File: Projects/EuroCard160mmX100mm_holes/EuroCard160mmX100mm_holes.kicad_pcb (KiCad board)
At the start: 2 copper layers, 159.9 x 99.9 mm, 4 parts

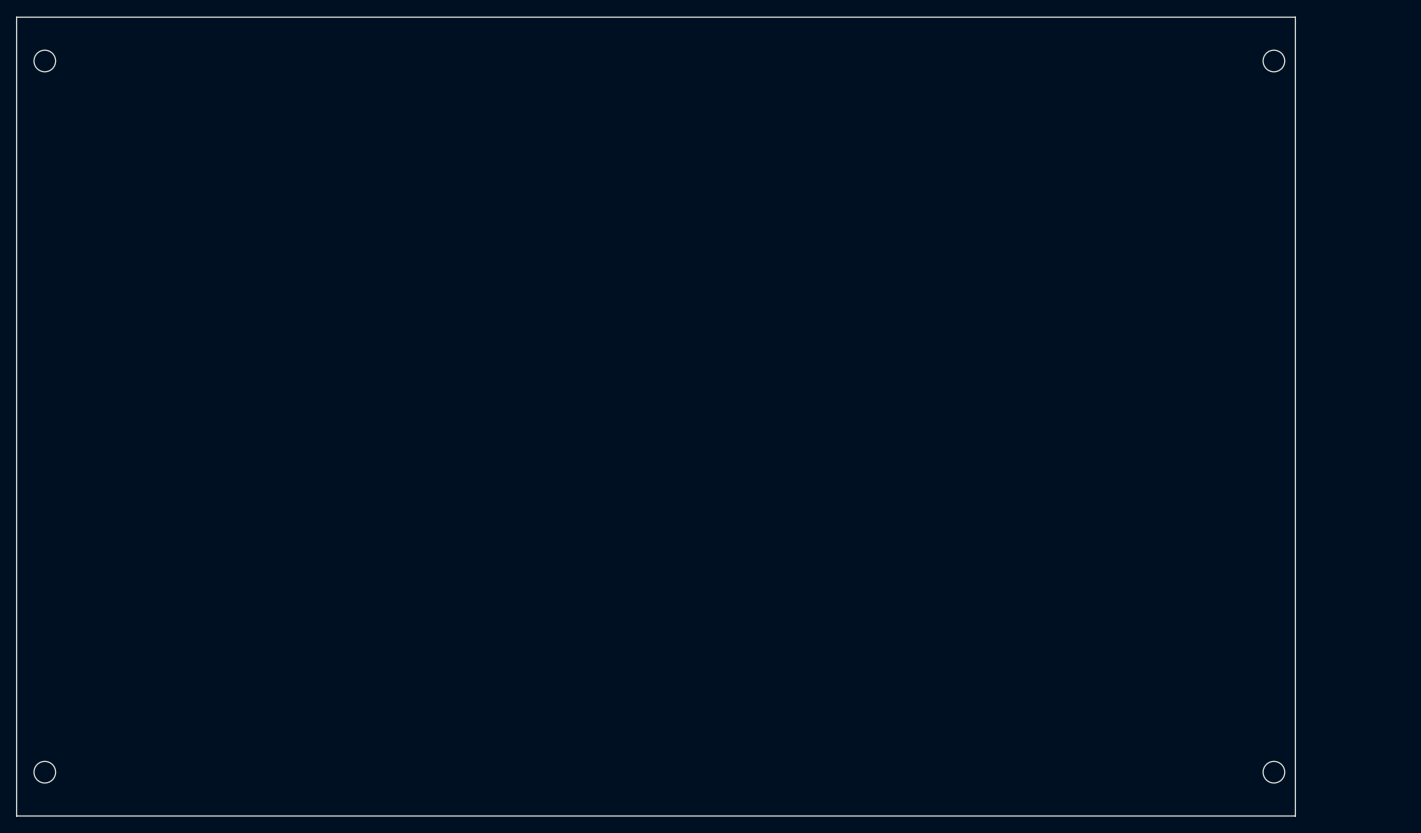
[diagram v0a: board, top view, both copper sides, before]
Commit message: Update EuroCard160mmX100mm* using KiCad 5.1.6
* Repointed all symbols and footprints to current libraries.
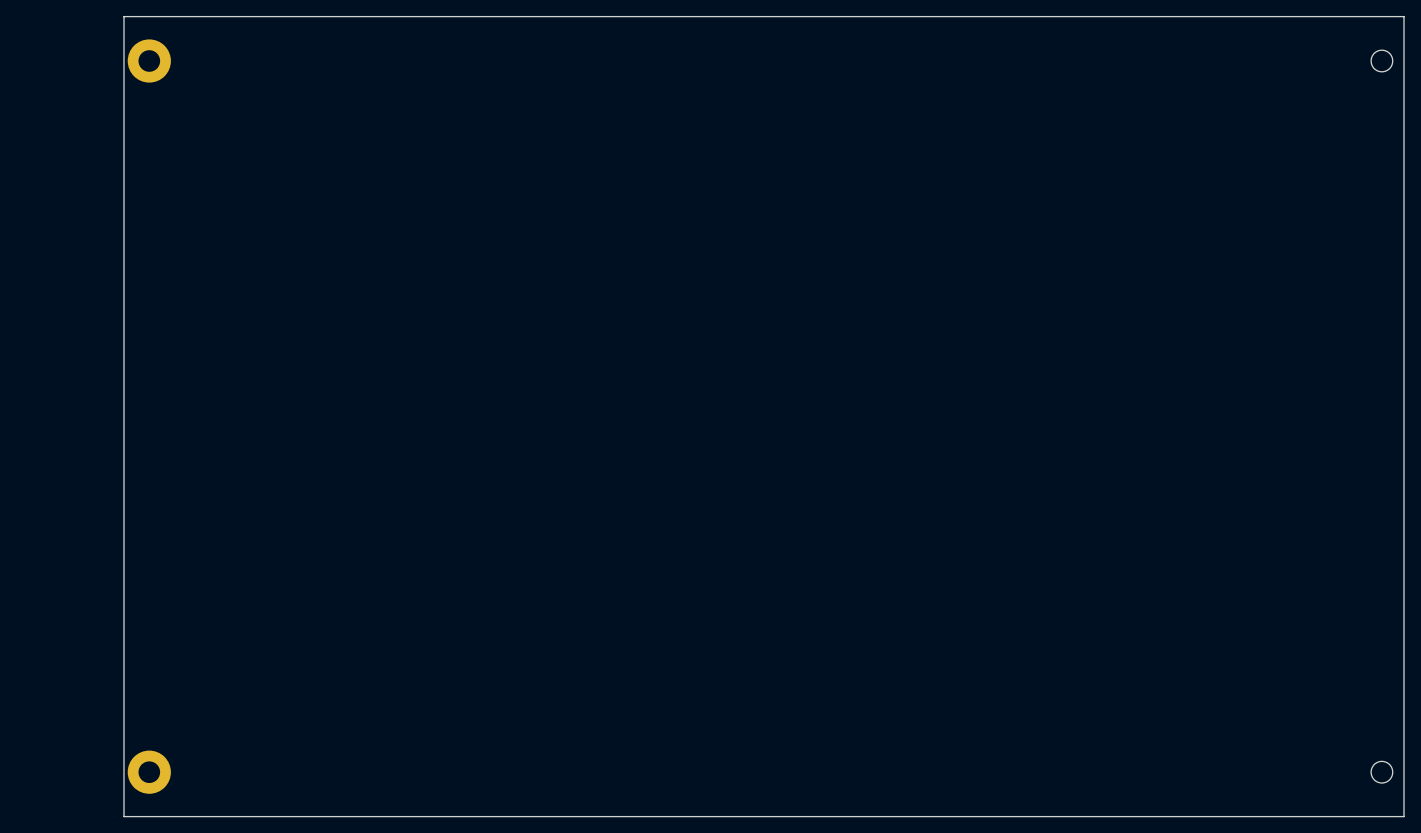
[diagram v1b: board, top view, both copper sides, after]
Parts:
- H1: renamed from MK2; value Mounting_Hole_PAD -> MountingHole; footprint Mounting_Holes:MountingHole_2.7mm -> MountingHole:MountingHole_2.7mm
- H2: renamed from MK4; value Mounting_Hole_PAD -> MountingHole; footprint Mounting_Holes:MountingHole_2.7mm -> MountingHole:MountingHole_2.7mm
- MK1: value Mounting_Hole_PAD -> MountingHole_Pad; footprint Mounting_Holes:MountingHole_2.7mm -> MountingHole:MountingHole_2.7mm_Pad
- MK2: renamed from MK3; value Mounting_Hole_PAD -> MountingHole_Pad; footprint Mounting_Holes:MountingHole_2.7mm -> MountingHole:MountingHole_2.7mm_Pad
- moved H1 13.5 mm to (225.7, 50.5)
- moved H2 13.5 mm to (225.7, 139.4)
- moved MK1 13.1 mm to (71.7, 50.5)
- moved MK2 13.1 mm to (71.7, 139.4)
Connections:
- H1 pad 1: Net-(MK2-Pad1) -> (no net)
- H2 pad 1: Net-(MK4-Pad1) -> (no net)
- MK1 pad 1: Net-(MK1-Pad1) -> (no net)
- MK2 pad 1: Net-(MK3-Pad1) -> (no net)
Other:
- board size 159.9 x 99.9 mm -> 160 x 100 mm
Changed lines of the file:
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@@
-(kicad_pcb (version 20171130) (host pcbnew no-vcs-found-c6d0075~61~ubuntu16.04.1)
+(kicad_pcb (version 20171130) (host pcbnew "(5.1.6)-1")
   (general
     (thickness 1.6)
@@
     (zones 0)
     (modules 4)
-    (nets 5)
+    (nets 1)
   )
   (page A4)
@@
     (zone_45_only no)
     (trace_min 0.2)
-    (segment_width 0.2)
-    (edge_width 0.15)
     (via_size 0.8)
     (via_drill 0.4)
@@
     (uvia_min_size 0.2)
     (uvia_min_drill 0.1)
+    (edge_width 0.15)
+    (segment_width 0.2)
     (pcb_text_width 0.3)
     (pcb_text_size 1.5 1.5)
@@
     (pad_to_mask_clearance 0.2)
     (aux_axis_origin 0 0)
-    (grid_origin 55.08 144.93)
-    (visible_elements FFFFFFFF)
+    (grid_origin 68.5 45)
+    (visible_elements 7FFFFFFF)
     (pcbplotparams
       (layerselection 0x00030_ffffffff)
@@
       (hpglpennumber 1)
       (hpglpenspeed 20)
-      (hpglpendiameter 15)
+      (hpglpendiameter 15.000000)
       (psnegative false)
       (psa4output false)
@@
   )
   (net 0 "")
-  (net 1 "Net-(MK1-Pad1)")
-  (net 2 "Net-(MK2-Pad1)")
-  (net 3 "Net-(MK3-Pad1)")
-  (net 4 "Net-(MK4-Pad1)")
   (net_class Default "This is the default net class."
     (clearance 0.2)
@@
     (add_net "Net-(MK1-Pad1)")
     (add_net "Net-(MK2-Pad1)")
-    (add_net "Net-(MK3-Pad1)")
-    (add_net "Net-(MK4-Pad1)")
-  )
-  (module Mounting_Holes:MountingHole_2.7mm (layer F.Cu)
-    (at 58.6 139.45)
+  )
+  (module MountingHole:MountingHole_2.7mm locked (layer F.Cu)
+    (at 225.74 139.45)
     (descr "Mounting Hole 2.7mm, no annular")
     (tags "mounting hole 2.7mm no annular")
-    (fp_text reference MK3 (at 0 -3.7) (layer F.SilkS) hide
-      (effects (font (size 1 1) (thickness 0.15)))
-    )
-    (fp_text value Mounting_Hole_PAD (at 0 3.7) (layer F.Fab) hide
-      (effects (font (size 1 1) (thickness 0.15)))
-    )
-    (fp_circle (center 0 0) (end 2.7 0) (layer Cmts.User) (width 0.15))
-    (fp_circle (center 0 0) (end 2.95 0) (layer F.CrtYd) (width 0.05))
-    (pad 1 np_thru_hole circle (at 0 0) (size 2.7 2.7) (drill 2.7) (layers *.Cu *.Mask)
-      (net 3 "Net-(MK3-Pad1)"))
-  )
-  (module Mounting_Holes:MountingHole_2.7mm (layer F.Cu)
-    (at 58.6 50.55)
+    (attr virtual)
+    (fp_text reference H2 (at 0 -3.7) (layer F.SilkS) hide
+      (effects (font (size 1 1) (thickness 0.15)))
+    )
+    (fp_text value MountingHole (at 0 3.7) (layer F.Fab)
+      (effects (font (size 1 1) (thickness 0.15)))
+    )
+    (fp_circle (center 0 0) (end 2.7 0) (layer Cmts.User) (width 0.15))
+    (fp_circle (center 0 0) (end 2.95 0) (layer F.CrtYd) (width 0.05))
+    (fp_text user %R (at 0.3 0) (layer F.Fab) hide
+      (effects (font (size 1 1) (thickness 0.15)))
+    )
+    (pad 1 np_thru_hole circle (at 0 0) (size 2.7 2.7) (drill 2.7) (layers *.Cu *.Mask))
+  )
+  (module MountingHole:MountingHole_2.7mm locked (layer F.Cu)
+    (at 225.74 50.55)
     (descr "Mounting Hole 2.7mm, no annular")
     (tags "mounting hole 2.7mm no annular")
+    (attr virtual)
+    (fp_text reference H1 (at 0 -3.7) (layer F.SilkS) hide
+      (effects (font (size 1 1) (thickness 0.15)))
+    )
+    (fp_text value MountingHole (at 0 3.7) (layer F.Fab)
+      (effects (font (size 1 1) (thickness 0.15)))
+    )
+    (fp_circle (center 0 0) (end 2.7 0) (layer Cmts.User) (width 0.15))
+    (fp_circle (center 0 0) (end 2.95 0) (layer F.CrtYd) (width 0.05))
+    (fp_text user %R (at 0.3 0) (layer F.Fab) hide
+      (effects (font (size 1 1) (thickness 0.15)))
+    )
+    (pad 1 np_thru_hole circle (at 0 0) (size 2.7 2.7) (drill 2.7) (layers *.Cu *.Mask))
+  )
+  (module MountingHole:MountingHole_2.7mm_Pad (layer F.Cu)
+    (at 71.665 50.55)
+    (descr "Mounting Hole 2.7mm")
+    (tags "mounting hole 2.7mm")
+    (attr virtual)
     (fp_text reference MK1 (at 0 -3.7) (layer F.SilkS) hide
       (effects (font (size 1 1) (thickness 0.15)))
     )
-    (fp_text value Mounting_Hole_PAD (at 0 3.7) (layer F.Fab) hide
-      (effects (font (size 1 1) (thickness 0.15)))
-    )
-    (fp_circle (center 0 0) (end 2.7 0) (layer Cmts.User) (width 0.15))
-    (fp_circle (center 0 0) (end 2.95 0) (layer F.CrtYd) (width 0.05))
-    (pad 1 np_thru_hole circle (at 0 0) (size 2.7 2.7) (drill 2.7) (layers *.Cu *.Mask)
-      (net 1 "Net-(MK1-Pad1)"))
-  )
-  (module Mounting_Holes:MountingHole_2.7mm (layer F.Cu)
-    (at 212.24 139.45)
-    (descr "Mounting Hole 2.7mm, no annular")
-    (tags "mounting hole 2.7mm no annular")
-    (fp_text reference MK4 (at 0 -3.7) (layer F.SilkS) hide
-      (effects (font (size 1 1) (thickness 0.15)))
-    )
-    (fp_text value Mounting_Hole_PAD (at 0 3.7) (layer F.Fab) hide
-      (effects (font (size 1 1) (thickness 0.15)))
-    )
-    (fp_circle (center 0 0) (end 2.7 0) (layer Cmts.User) (width 0.15))
-    (fp_circle (center 0 0) (end 2.95 0) (layer F.CrtYd) (width 0.05))
-    (pad 1 np_thru_hole circle (at 0 0) (size 2.7 2.7) (drill 2.7) (layers *.Cu *.Mask)
-      (net 4 "Net-(MK4-Pad1)"))
-  )
-  (module Mounting_Holes:MountingHole_2.7mm (layer F.Cu)
-    (at 212.24 50.55)
-    (descr "Mounting Hole 2.7mm, no annular")
-    (tags "mounting hole 2.7mm no annular")
+    (fp_text value MountingHole_Pad (at 0 3.7) (layer F.Fab)
+      (effects (font (size 1 1) (thickness 0.15)))
+    )
+    (fp_circle (center 0 0) (end 2.95 0) (layer F.CrtYd) (width 0.05))
+    (fp_circle (center 0 0) (end 2.7 0) (layer Cmts.User) (width 0.15))
+    (fp_text user %R (at 0.3 0) (layer F.Fab) hide
+      (effects (font (size 1 1) (thickness 0.15)))
+    )
+    (pad 1 thru_hole circle (at 0 0) (size 5.4 5.4) (drill 2.7) (layers *.Cu *.Mask))
+  )
+  (module MountingHole:MountingHole_2.7mm_Pad (layer F.Cu)
+    (at 71.665 139.45)
+    (descr "Mounting Hole 2.7mm")
+    (tags "mounting hole 2.7mm")
+    (attr virtual)
     (fp_text reference MK2 (at 0 -3.7) (layer F.SilkS) hide
       (effects (font (size 1 1) (thickness 0.15)))
     )
-    (fp_text value Mounting_Hole_PAD (at 0 3.7) (layer F.Fab) hide
-      (effects (font (size 1 1) (thickness 0.15)))
-    )
-    (fp_circle (center 0 0) (end 2.7 0) (layer Cmts.User) (width 0.15))
-    (fp_circle (center 0 0) (end 2.95 0) (layer F.CrtYd) (width 0.05))
-    (pad 1 np_thru_hole circle (at 0 0) (size 2.7 2.7) (drill 2.7) (layers *.Cu *.Mask)
-      (net 2 "Net-(MK2-Pad1)"))
-  )
-  (gr_line (start 214.9 47.5) (end 55.1 47.5) (angle 90) (layer F.CrtYd) (width 0.2))
-  (gr_line (start 55.1 47.5) (end 214.9 47.5) (angle 90) (layer B.CrtYd) (width 0.2))
-  (gr_line (start 55.1 142.5) (end 214.9 142.5) (angle 90) (layer B.CrtYd) (width 0.2))
-  (gr_line (start 55.1 142.5) (end 214.9 142.5) (angle 90) (layer F.CrtYd) (width 0.2))
-  (gr_line (start 55.075 144.925) (end 214.925 144.925) (angle 90) (layer Edge.Cuts) (width 0.15))
-  (gr_line (start 55.075 45.075) (end 55.075 144.925) (angle 90) (layer Edge.Cuts) (width 0.15))
-  (gr_line (start 214.925 45.075) (end 55.075 45.075) (angle 90) (layer Edge.Cuts) (width 0.15))
-  (gr_line (start 214.925 144.925) (end 214.925 45.075) (angle 90) (layer Edge.Cuts) (width 0.15))
+    (fp_text value MountingHole_Pad (at 0 3.7) (layer F.Fab)
+      (effects (font (size 1 1) (thickness 0.15)))
+    )
+    (fp_circle (center 0 0) (end 2.95 0) (layer F.CrtYd) (width 0.05))
+    (fp_circle (center 0 0) (end 2.7 0) (layer Cmts.User) (width 0.15))
+    (fp_text user %R (at 0.3 0) (layer F.Fab) hide
+      (effects (font (size 1 1) (thickness 0.15)))
+    )
+    (pad 1 thru_hole circle (at 0 0) (size 5.4 5.4) (drill 2.7) (layers *.Cu *.Mask))
+  )
+  (gr_line (start 228.5 47.4) (end 68.5 47.4) (angle 90) (layer F.CrtYd) (width 0.2))
+  (gr_line (start 68.5 47.4) (end 228.5 47.4) (angle 90) (layer B.CrtYd) (width 0.2))
+  (gr_line (start 68.5 142.6) (end 228.5 142.6) (angle 90) (layer B.CrtYd) (width 0.2))
+  (gr_line (start 68.5 142.6) (end 228.5 142.6) (angle 90) (layer F.CrtYd) (width 0.2))
+  (gr_line (start 68.5 145) (end 228.5 145) (angle 90) (layer Edge.Cuts) (width 0.15))
+  (gr_line (start 68.5 45) (end 68.5 145) (angle 90) (layer Edge.Cuts) (width 0.15))
+  (gr_line (start 228.5 45) (end 68.5 45) (angle 90) (layer Edge.Cuts) (width 0.15))
+  (gr_line (start 228.5 145) (end 228.5 45) (angle 90) (layer Edge.Cuts) (width 0.15))
+  (zone (net 0) (net_name "") (layers F&B.Cu) (hatch full 0.508)
+    (connect_pads (clearance 0.508))
+    (min_thickness 0.254)
+    (keepout (tracks not_allowed) (vias not_allowed) (copperpour not_allowed))
+    (fill (arc_segments 32) (thermal_gap 0.508) (thermal_bridge_width 0.508))
+    (polygon
+      (pts
+        (xy 228.5 47.5) (xy 68.5 47.5) (xy 68.5 45) (xy 228.5 45)
+      )
+    )
+  )
+  (zone (net 0) (net_name "") (layers F&B.Cu) (hatch full 0.508)
+    (connect_pads (clearance 0.508))
+    (min_thickness 0.254)
+    (keepout (tracks not_allowed) (vias not_allowed) (copperpour not_allowed))
+    (fill (arc_segments 32) (thermal_gap 0.508) (thermal_bridge_width 0.508))
+    (polygon
+      (pts
+        (xy 228.5 145) (xy 68.5 145) (xy 68.5 142.5) (xy 228.5 142.5)
+      )
+    )
+  )
 )
